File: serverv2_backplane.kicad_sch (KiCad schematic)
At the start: 0 parts

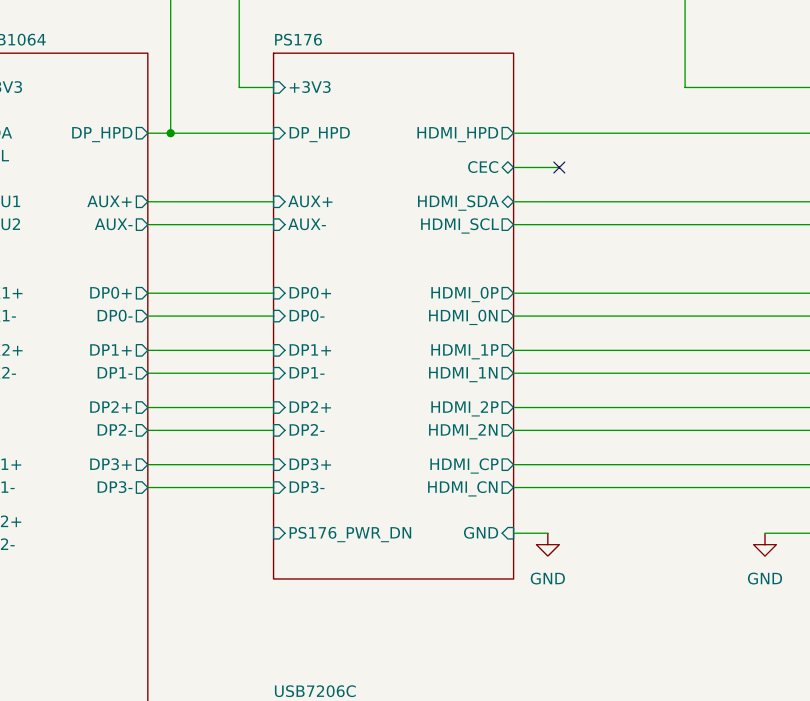
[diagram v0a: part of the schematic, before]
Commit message: Cleaned up PS176 schematic and added some datasheets
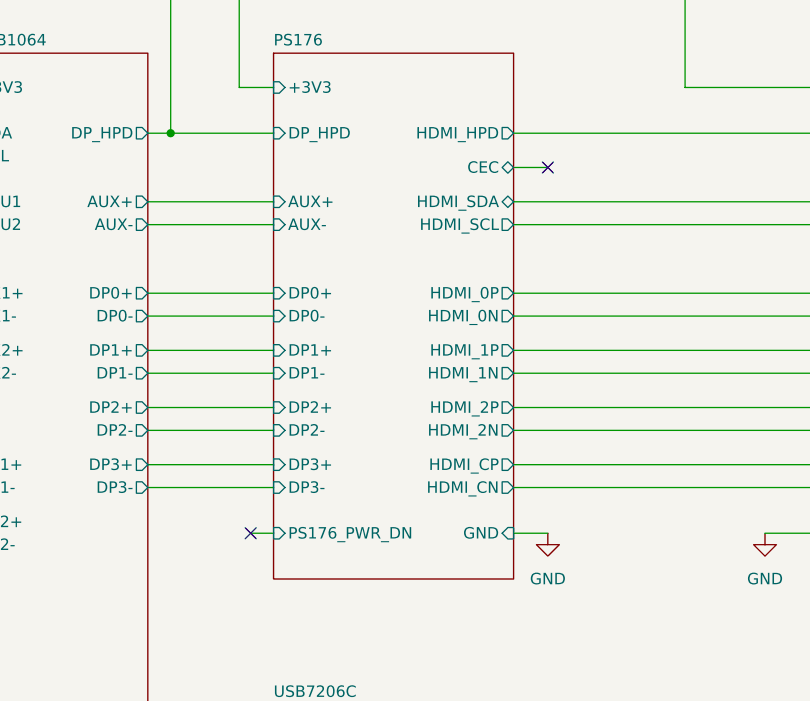
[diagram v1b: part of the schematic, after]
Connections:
- no-connect marks 16 -> 17
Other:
- company: (none) -> By: Matthew Kong
- title: (none) -> LAZARUS-1 Backplane PCB
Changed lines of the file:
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@@
 	(generator_version "10.0")
 	(paper "A2" portrait)
+	(title_block
+		(title "LAZARUS-1 Backplane PCB")
+		(date "2026-07-21")
+		(rev "1.0")
+		(company "By: Matthew Kong")
+	)
 	(text "SATA_12V_FLT_10"
 		(exclude_from_sim no)
@@
 	)
 	(no_connect
-		(at 124.46 241.3)
+		(at 123.19 241.3)
 	)
 	(no_connect
@@
 	)
 	(no_connect
+		(at 90.17 281.94)
+	)
+	(no_connect
 		(at 271.78 232.41)
 	)
@@
 	(wire
 		(pts
+			(xy 90.17 281.94) (xy 92.71 281.94)
+		)
+		(stroke
+			(width 0)
+			(type default)
+		)
+	)
+	(wire
+		(pts
 			(xy 330.2 182.88) (xy 356.87 182.88)
 		)
@@
 	(wire
 		(pts
-			(xy 119.38 241.3) (xy 124.46 241.3)
+			(xy 119.38 241.3) (xy 123.19 241.3)
 		)
 		(stroke

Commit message: Basic function review and documentation for PS176 subsystem
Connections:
- no-connect marks 17 -> 15
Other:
- sheet PS176 ports: added +5V; removed none
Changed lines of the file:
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@@
 	)
 	(no_connect
-		(at 271.78 391.16)
-	)
-	(no_connect
 		(at 123.19 241.3)
 	)
@@
 	)
 	(no_connect
-		(at 90.17 281.94)
-	)
-	(no_connect
 		(at 271.78 232.41)
 	)
@@
 	(wire
 		(pts
+			(xy 91.44 281.94) (xy 92.71 281.94)
+		)
+		(stroke
+			(width 0)
+			(type default)
+		)
+	)
+	(wire
+		(pts
 			(xy 170.18 173.99) (xy 292.1 173.99)
 		)
@@
 	(wire
 		(pts
-			(xy 119.38 318.77) (xy 152.4 318.77)
+			(xy 276.86 391.16) (xy 278.13 391.16)
 		)
 		(stroke
 			(width 0)
 			(type default)
+			(color 118 118 118 1)
 		)
 	)
 	(wire
 		(pts
-			(xy 389.255 30.48) (xy 393.7 30.48)
+			(xy 119.38 318.77) (xy 152.4 318.77)
 		)
 		(stroke
@@
 	(wire
 		(pts
-			(xy 90.17 281.94) (xy 92.71 281.94)
+			(xy 389.255 30.48) (xy 393.7 30.48)
 		)
 		(stroke
@@
 	(wire
 		(pts
+			(xy 91.44 281.94) (xy 92.71 281.94)
+		)
+		(stroke
+			(width 0)
+			(type default)
+			(color 118 118 118 1)
+		)
+	)
+	(wire
+		(pts
 			(xy 238.76 40.64) (xy 356.87 40.64)
 		)
@@
 	(wire
 		(pts
+			(xy 123.19 232.41) (xy 119.38 232.41)
+		)
+		(stroke
+			(width 0)
+			(type default)
+		)
+	)
+	(wire
+		(pts
+			(xy 123.19 229.87) (xy 123.19 232.41)
+		)
+		(stroke
+			(width 0)
+			(type default)
+		)
+	)
+	(wire
+		(pts
 			(xy 295.91 143.51) (xy 302.26 143.51)
 		)
@@
 	(wire
 		(pts
-			(xy 271.78 391.16) (xy 278.13 391.16)
-		)
-		(stroke
-			(width 0)
-			(type default)
-		)
-	)
-	(wire
-		(pts
 			(xy 238.76 27.94) (xy 356.87 27.94)
 		)
@@
 		)
 	)
+	(global_label "PS176_EN"
+		(shape input)
+		(at 91.44 281.94 180)
+		(fields_autoplaced yes)
+		(effects
+			(font
+				(size 1.27 1.27)
+				(color 118 118 118 1)
+			)
+			(justify right)
+		)
+		(property "Intersheetrefs" "${INTERSHEET_REFS}"
+			(at 78.8997 281.94 0)
+			(hide yes)
+			(show_name no)
+			(do_not_autoplace no)
+			(effects
+				(font
+					(size 1.27 1.27)
+				)
+				(justify right)
+			)
+		)
+	)
 	(global_label "SDA3"
 		(shape bidirectional)
@@
 		)
 	)
+	(global_label "PS176_EN"
+		(shape output)
+		(at 276.86 391.16 180)
+		(fields_autoplaced yes)
+		(effects
+			(font
+				(size 1.27 1.27)
+				(color 118 118 118 1)
+			)
+			(justify right)
+		)
+		(property "Intersheetrefs" "${INTERSHEET_REFS}"
+			(at 264.3197 391.16 0)
+			(hide yes)
+			(show_name no)
+			(do_not_autoplace no)
+			(effects
+				(font
+					(size 1.27 1.27)
+				)
+				(justify right)
+			)
+		)
+	)
 	(global_label "SDA3"
 		(shape bidirectional)
@@
 		)
 	)
+	(symbol
+		(lib_id "power:+5V")
+		(at 123.19 229.87 0)
+		(unit 1)
+		(body_style 1)
+		(exclude_from_sim no)
+		(in_bom yes)
+		(on_board yes)
+		(in_pos_files yes)
+		(dnp no)
+		(fields_autoplaced yes)
+		(property "Reference" "#PWR0514"
+			(at 123.19 233.68 0)
+			(hide yes)
+			(show_name no)
+			(do_not_autoplace no)
+			(effects
+				(font
+					(size 1.27 1.27)
+				)
+			)
+		)
+		(property "Value" "+5V"
+			(at 123.19 224.79 0)
+			(show_name no)
+			(do_not_autoplace no)
+			(effects
+				(font
+					(size 1.27 1.27)
+				)
+			)
+		)
+		(property "Footprint" ""
+			(at 123.19 229.87 0)
+			(hide yes)
+			(show_name no)
+			(do_not_autoplace no)
+			(effects
+				(font
+					(size 1.27 1.27)
+				)
+			)
+		)
+		(property "Datasheet" ""
+			(at 123.19 229.87 0)
+			(hide yes)
+			(show_name no)
+			(do_not_autoplace no)
+			(effects
+				(font
+					(size 1.27 1.27)
+				)
+			)
+		)
+		(property "Description" "Power symbol creates a global label with name \"+5V\""
+			(at 123.19 229.87 0)
+			(hide yes)
+			(show_name no)
+			(do_not_autoplace no)
+			(effects
+				(font
+					(size 1.27 1.27)
+				)
+			)
+		)
+		(pin "1"
+		)
+		(instances
+			(project "serverv2_backplane"
+				(path "/d38d6818-cf53-410d-afa3-a75a85b7c05a"
+					(reference "#PWR0514")
+					(unit 1)
+				)
+			)
+		)
+	)
 	(sheet
 		(at 278.13 186.69)
@@
 			(effects
 				(font
+					(size 1.27 1.27)
+				)
+				(justify right)
+			)
+		)
+		(pin "+5V" input
+			(at 119.38 232.41 0)
+			(effects
+				(font

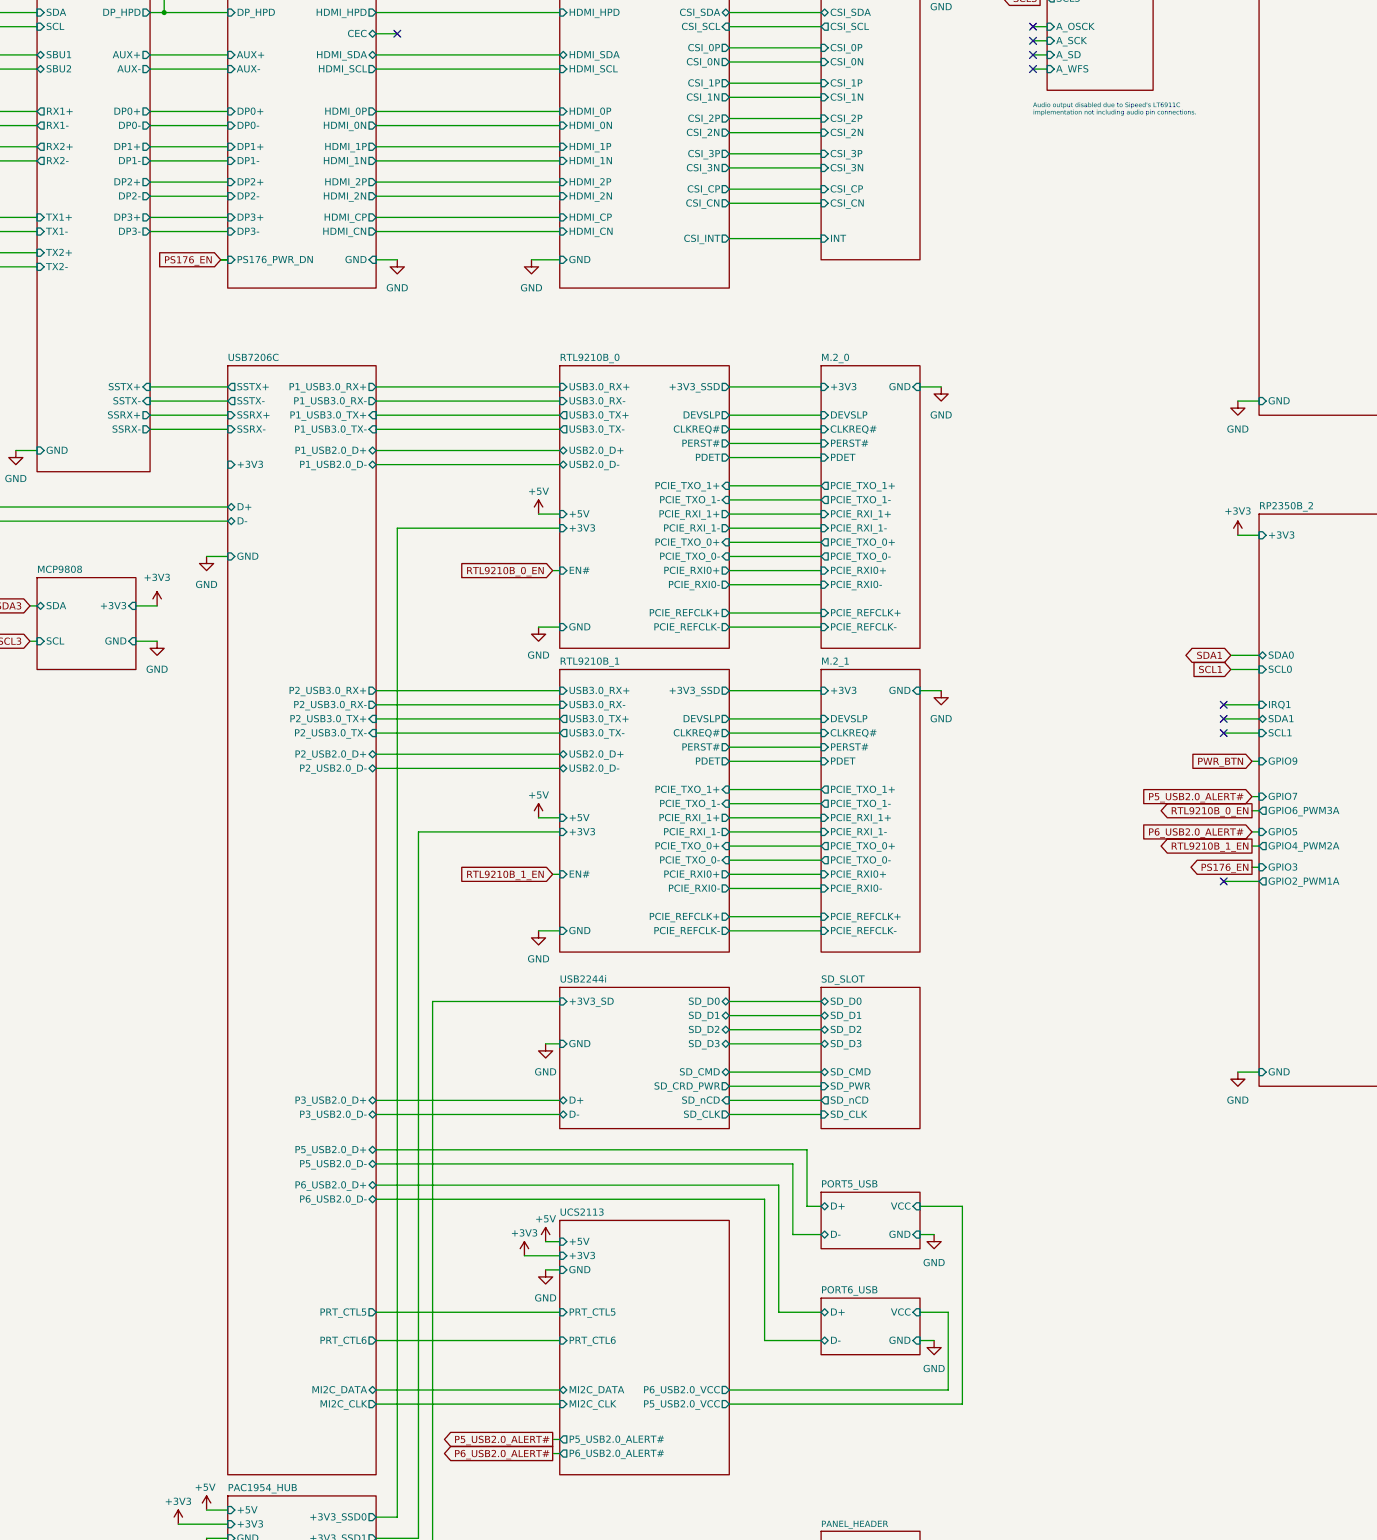
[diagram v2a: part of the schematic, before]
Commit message: Added TVS clamping diodes to upstream USB-C port and fixed RX/TX orientation routing for entire system
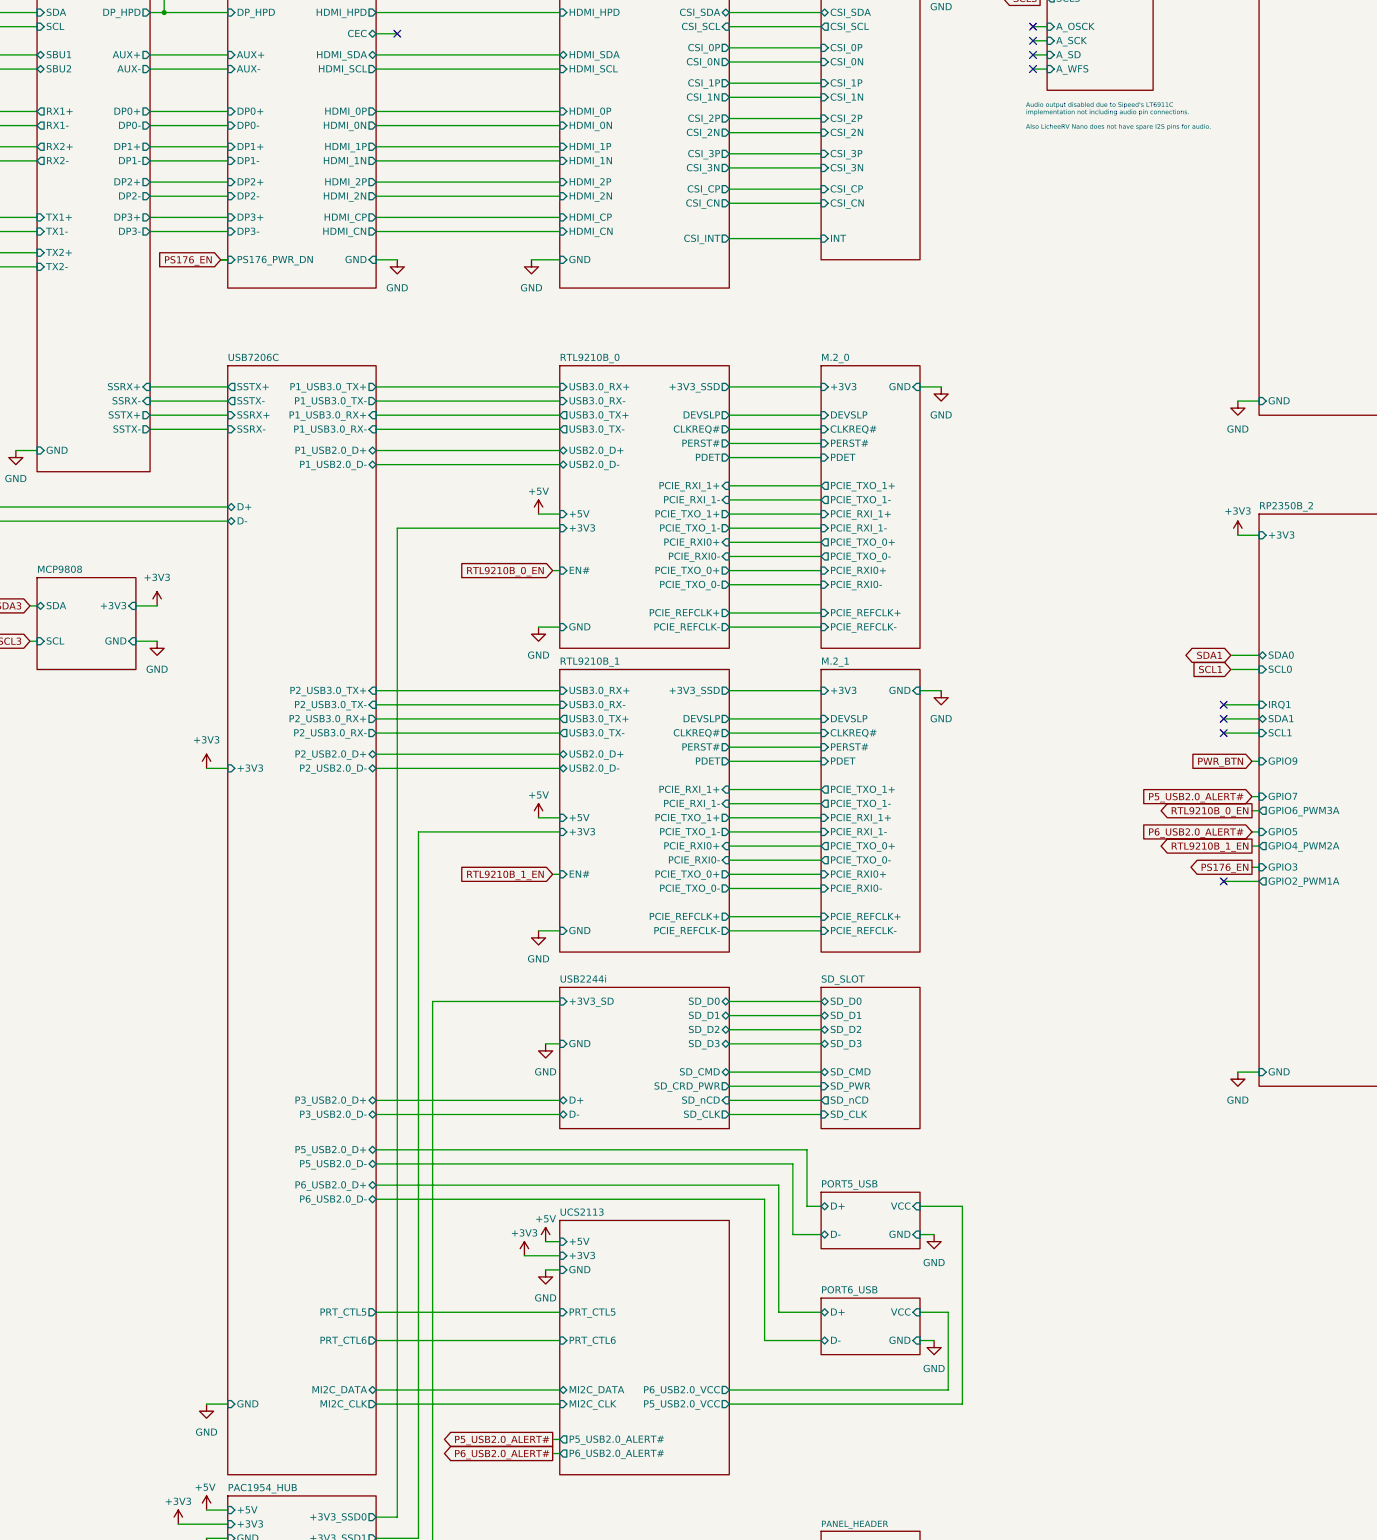
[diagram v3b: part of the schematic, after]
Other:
- note added: "Audio output disabled due to Sipeed's LT6911C implementation not including audio pin connections. Also LicheeRV Nano does not have spare I2S pins for audio."
- note removed: "Audio output disabled due to Sipeed's LT6911C implementation not including audio pin connections."

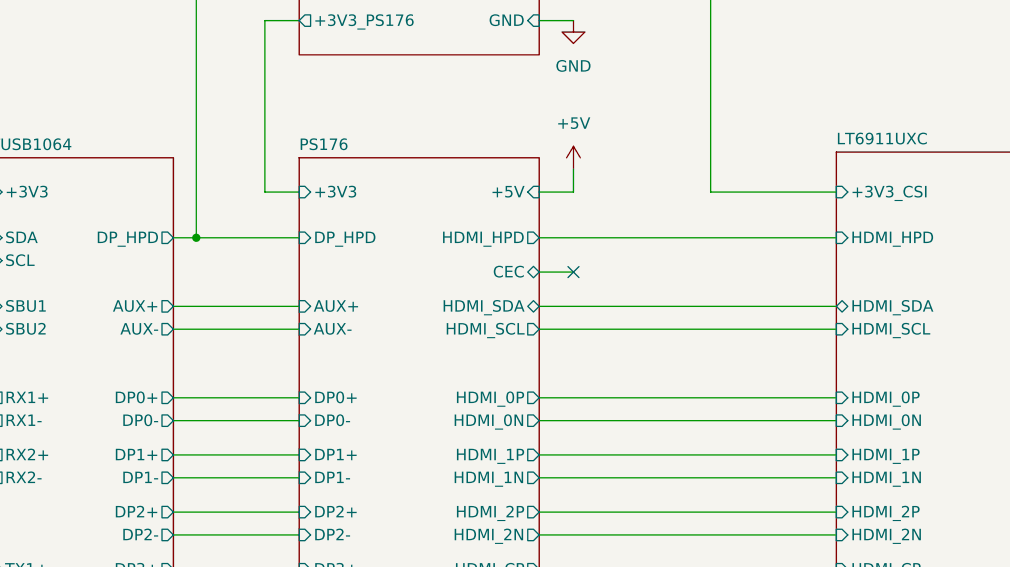
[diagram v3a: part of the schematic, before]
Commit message: Basic Function Review and Documentation for TUSB1064 subsystem
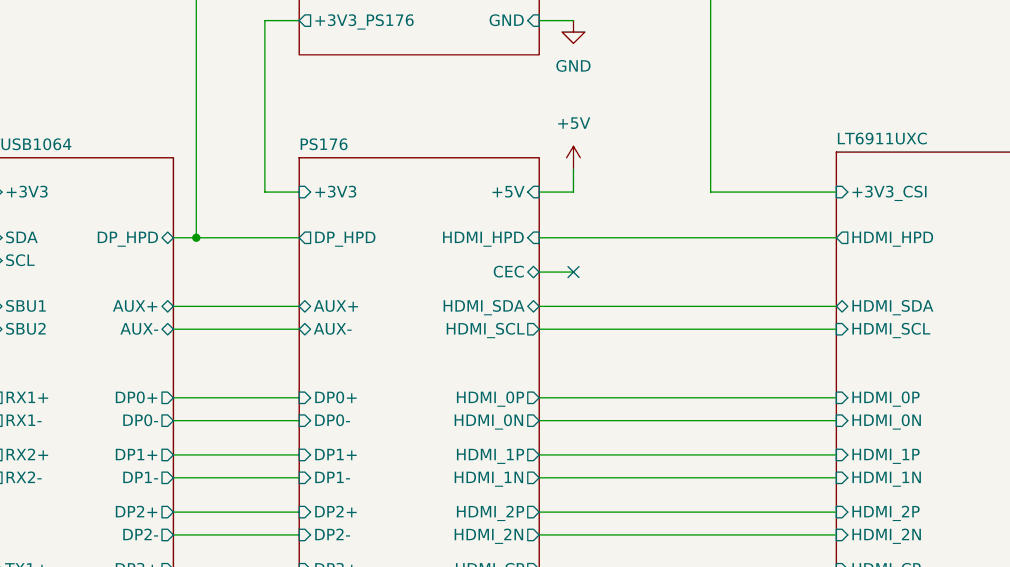
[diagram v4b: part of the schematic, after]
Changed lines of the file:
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@@
 			)
 		)
-		(pin "HDMI_HPD" input
+		(pin "HDMI_HPD" output
 			(at 152.4 237.49 180)
 			(effects
@@
 			)
 		)
-		(pin "DP_HPD" output
+		(pin "DP_HPD" bidirectional
 			(at 78.74 237.49 0)
 			(effects
@@
 			)
 		)
-		(pin "AUX+" output
+		(pin "AUX+" bidirectional
 			(at 78.74 245.11 0)
 			(effects
@@
 			)
 		)
-		(pin "AUX-" output
+		(pin "AUX-" bidirectional
 			(at 78.74 247.65 0)
 			(effects
@@
 			)
 		)
-		(pin "AUX-" input
+		(pin "AUX-" bidirectional
 			(at 92.71 247.65 180)
 			(effects
@@
 			)
 		)
-		(pin "HDMI_HPD" output
+		(pin "HDMI_HPD" input
 			(at 119.38 237.49 0)
 			(effects
@@
 			)
 		)
-		(pin "AUX+" input
+		(pin "AUX+" bidirectional
 			(at 92.71 245.11 180)
 			(effects
@@
 			)
 		)
-		(pin "DP_HPD" input
+		(pin "DP_HPD" output
 			(at 92.71 237.49 180)
 			(effects
